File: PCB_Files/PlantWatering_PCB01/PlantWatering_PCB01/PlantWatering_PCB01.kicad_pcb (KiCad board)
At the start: 2 copper layers, 109 x 55.5 mm, 54 parts, among them J1 Connector to PCB2, J13 USB_C_Receptacle_USB2.0_16P, J2 LED_Strip, J3 I2C, J4 Power, Q1 MUN5211DW1, SW1 SW_Push, SW2 SW_Push, SW3 SW_Push, SW4 SW_Push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

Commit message: changed PCB01
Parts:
- R18, R19, R39, R9: footprint Resistor_SMD:R_1206_3216Metric -> Resistor_SMD:R_0805_2012Metric
- moved R19 0.34 mm to (96.1, 122.4)
- renumbered TX to D4, RX to D5
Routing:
- net +3.3V: track 248.8 -> 249.8 mm
- net /LCD_RD: track 3.96 -> 4.85 mm

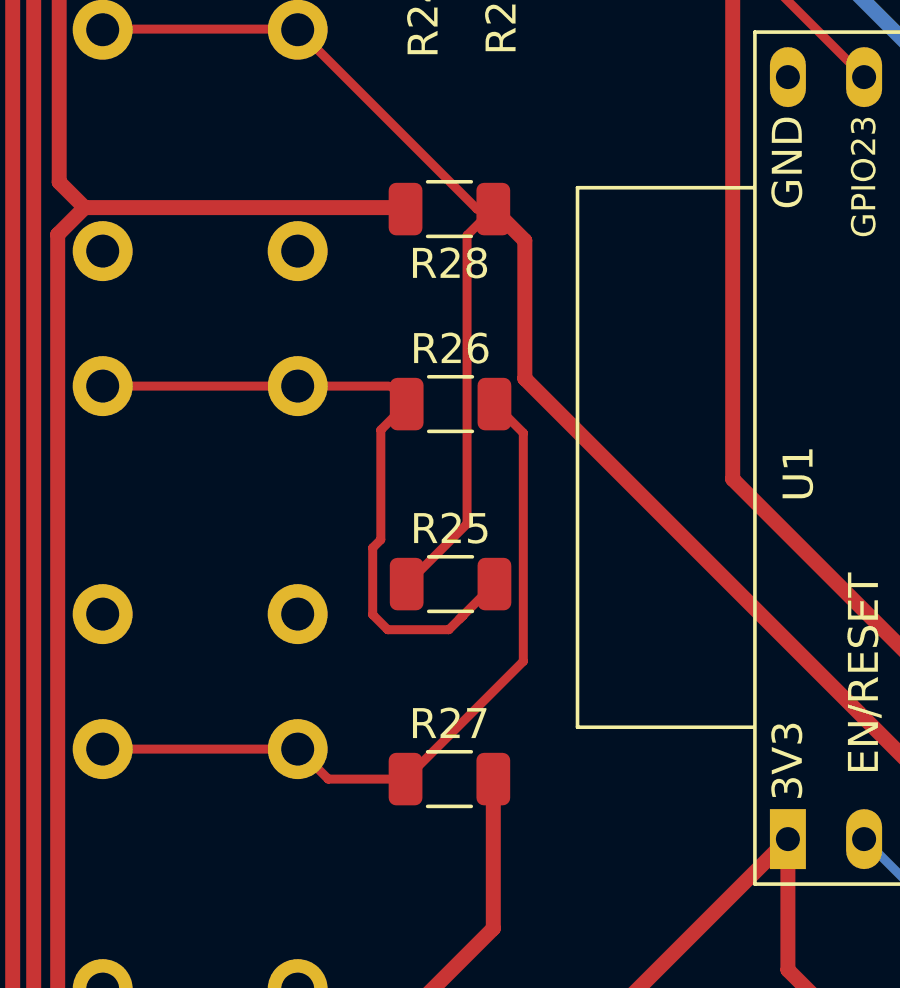
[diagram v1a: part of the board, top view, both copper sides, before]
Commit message: changed resistance of buttons (look at schematic)
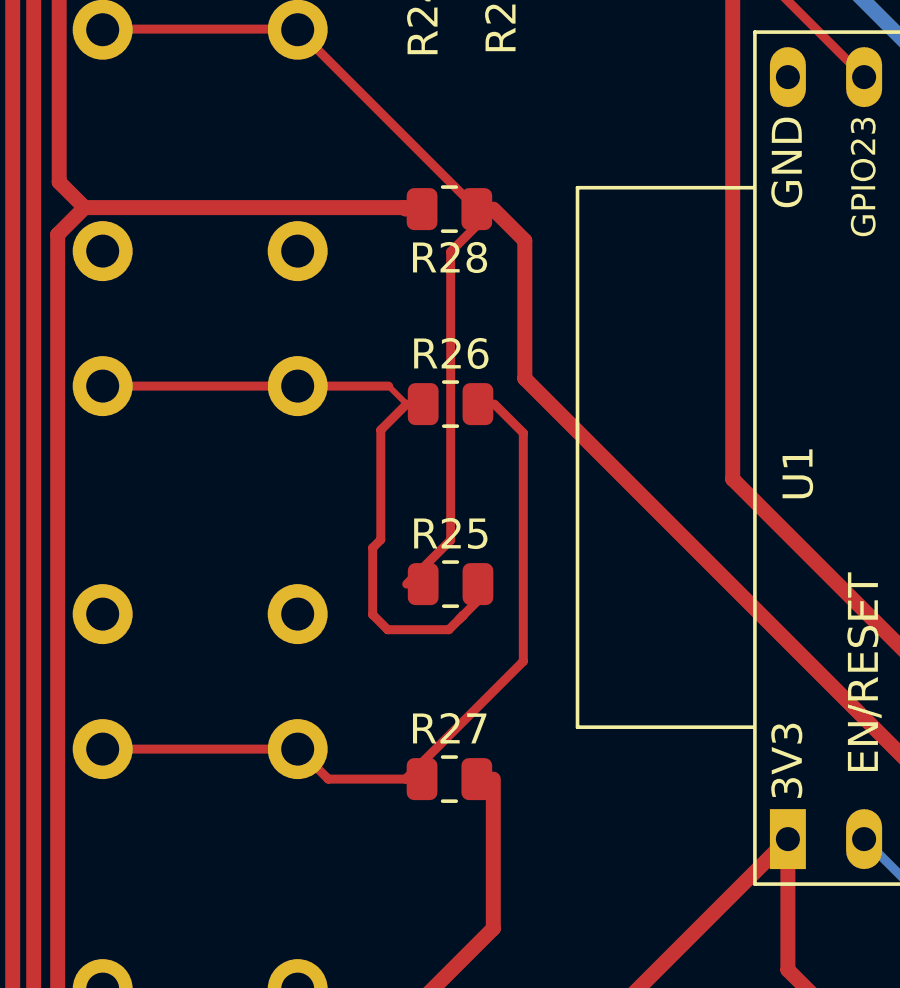
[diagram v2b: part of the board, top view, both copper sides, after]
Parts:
- R25, R26, R27: value 1k -> 10k; footprint Resistor_SMD:R_1206_3216Metric -> Resistor_SMD:R_0805_2012Metric
- R28: value 1k -> 62k; footprint Resistor_SMD:R_1206_3216Metric -> Resistor_SMD:R_0805_2012Metric
